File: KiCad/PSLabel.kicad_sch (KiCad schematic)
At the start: 0 parts

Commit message: Refactor code structure for improved readability and maintainability
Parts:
- added U1: nRF54L15-QFXX, Package_DFN_QFN:QFN-48-1EP_6x6mm_P0.4mm_EP4.6x4.6mm, symbol nordic-lib-kicad-nrf54l:nRF54L15-QFXX
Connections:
- new net: U1.10 (VDD), U1.22 (VDD), U1.36 (VDD), U1.47 (VDD), U1.48 (VDD)
- new net: U1.32 (VSS_PA), U1.44 (VSS), U1.49 (VSS)
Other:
- title: (none) -> PSLabel
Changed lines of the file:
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@@
 	(generator_version "9.0")
 	(paper "A4")
+	(title_block
+		(title "PSLabel")
+		(date "2025-06-19")
+	)
+	(symbol
+		(lib_id "nordic-lib-kicad-nrf54l:nRF54L15-QFXX")
+		(at 132.08 101.6 0)
+		(unit 1)
+		(exclude_from_sim no)
+		(in_bom yes)
+		(on_board yes)
+		(dnp no)
+		(fields_autoplaced yes)
+		(property "Reference" "U1"
+			(at 132.08 101.6 0)
+			(do_not_autoplace yes)
+			(effects
+				(font
+					(size 1.27 1.27)
+				)
+			)
+		)
+		(property "Value" "nRF54L15-QFXX"
+			(at 132.08 104.14 0)
+			(do_not_autoplace yes)
+			(effects
+				(font
+					(size 1.27 1.27)
+				)
+			)
+		)
+		(property "Footprint" "Package_DFN_QFN:QFN-48-1EP_6x6mm_P0.4mm_EP4.6x4.6mm"
+			(at 132.08 175.26 0)
+			(effects
+				(font
+					(size 1.27 1.27)
+				)
+				(hide yes)
+			)
+		)
+		(property "Datasheet" "https://docs.nordicsemi.com/bundle/ps_nrf54L15"
+			(at 132.08 177.8 0)
+			(effects
+				(font
+					(size 1.27 1.27)
+				)
+				(hide yes)
+			)
+		)
+		(property "Description" "nRF54L Dual Core Multiprotocol BLE SoC"
+			(at 132.08 172.72 0)
+			(effects
+				(font
+					(size 1.27 1.27)
+				)
+				(hide yes)
+			)
+		)
+		(pin "17"
+		)
+		(pin "15"
+		)
+		(pin "30"
+		)
+		(pin "10"
+		)
+		(pin "25"
+		)
+		(pin "9"
+		)
+		(pin "14"
+		)
+		(pin "1"
+		)
+		(pin "21"
+		)
+		(pin "43"
+		)
+		(pin "37"
+		)
+		(pin "20"
+		)
+		(pin "13"
+		)
+		(pin "12"
+		)
+		(pin "48"
+		)
+		(pin "36"
+		)
+		(pin "18"
+		)
+		(pin "2"
+		)
+		(pin "32"
+		)
+		(pin "41"
+		)
+		(pin "46"
+		)
+		(pin "31"
+		)
+		(pin "3"
+		)
+		(pin "33"
+		)
+		(pin "16"
+		)
+		(pin "39"
+		)
+		(pin "45"
+		)
+		(pin "40"
+		)
+		(pin "38"
+		)
+		(pin "47"
+		)
+		(pin "22"
+		)
+		(pin "23"
+		)
+		(pin "35"
+		)
+		(pin "34"
+		)
+		(pin "44"
+		)
+		(pin "49"
+		)
+		(pin "11"
+		)
+		(pin "26"
+		)
+		(pin "28"
+		)
+		(pin "7"
+		)
+		(pin "4"
+		)
+		(pin "6"
+		)
+		(pin "42"
+		)
+		(pin "8"
+		)
+		(pin "19"
+		)
+		(pin "5"
+		)
+		(pin "29"
+		)
+		(pin "24"
+		)
+		(pin "27"
+		)
+		(instances
+			(project ""
+				(path "/3e66aa7a-7b9f-4ef6-923c-a0fae49a7217"
+					(reference "U1")
+					(unit 1)
+				)
+			)
+		)
+	)
 	(sheet_instances
 		(path "/"

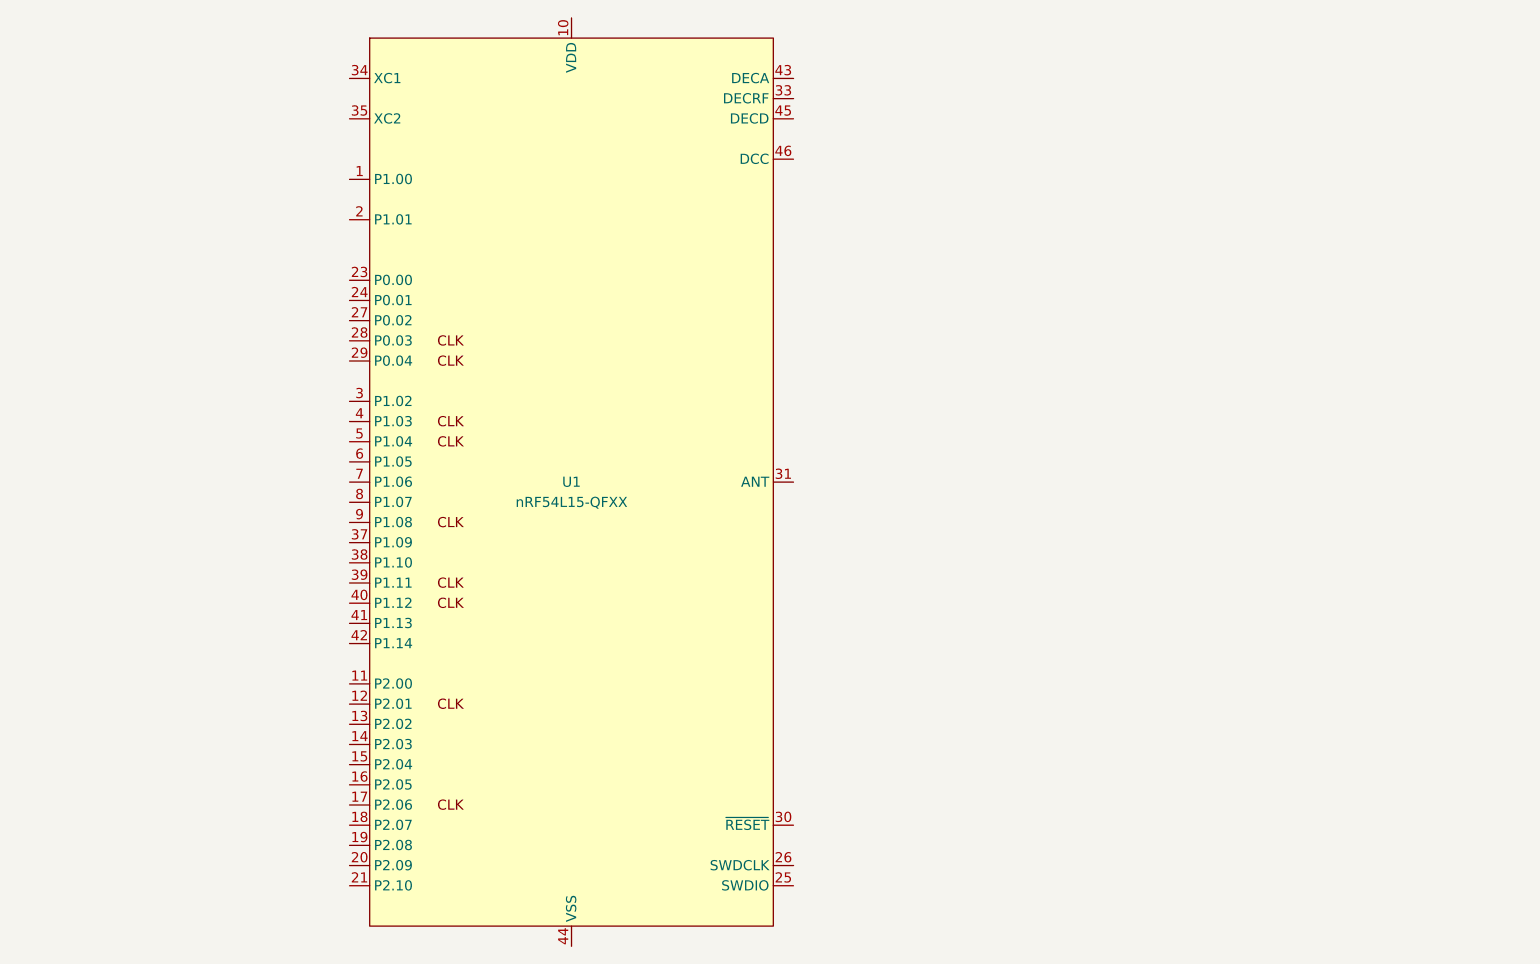
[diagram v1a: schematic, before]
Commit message: Add nRF54L15 schematic to KiCad project
- Introduced a new schematic file for the nRF54L15 component.
- Included detailed properties such as Reference, Value, Footprint, Datasheet, and Description.
- Defined multiple pins with their respective attributes and alternate functions.
- Ensured proper formatting and organization for readability and future modifications.
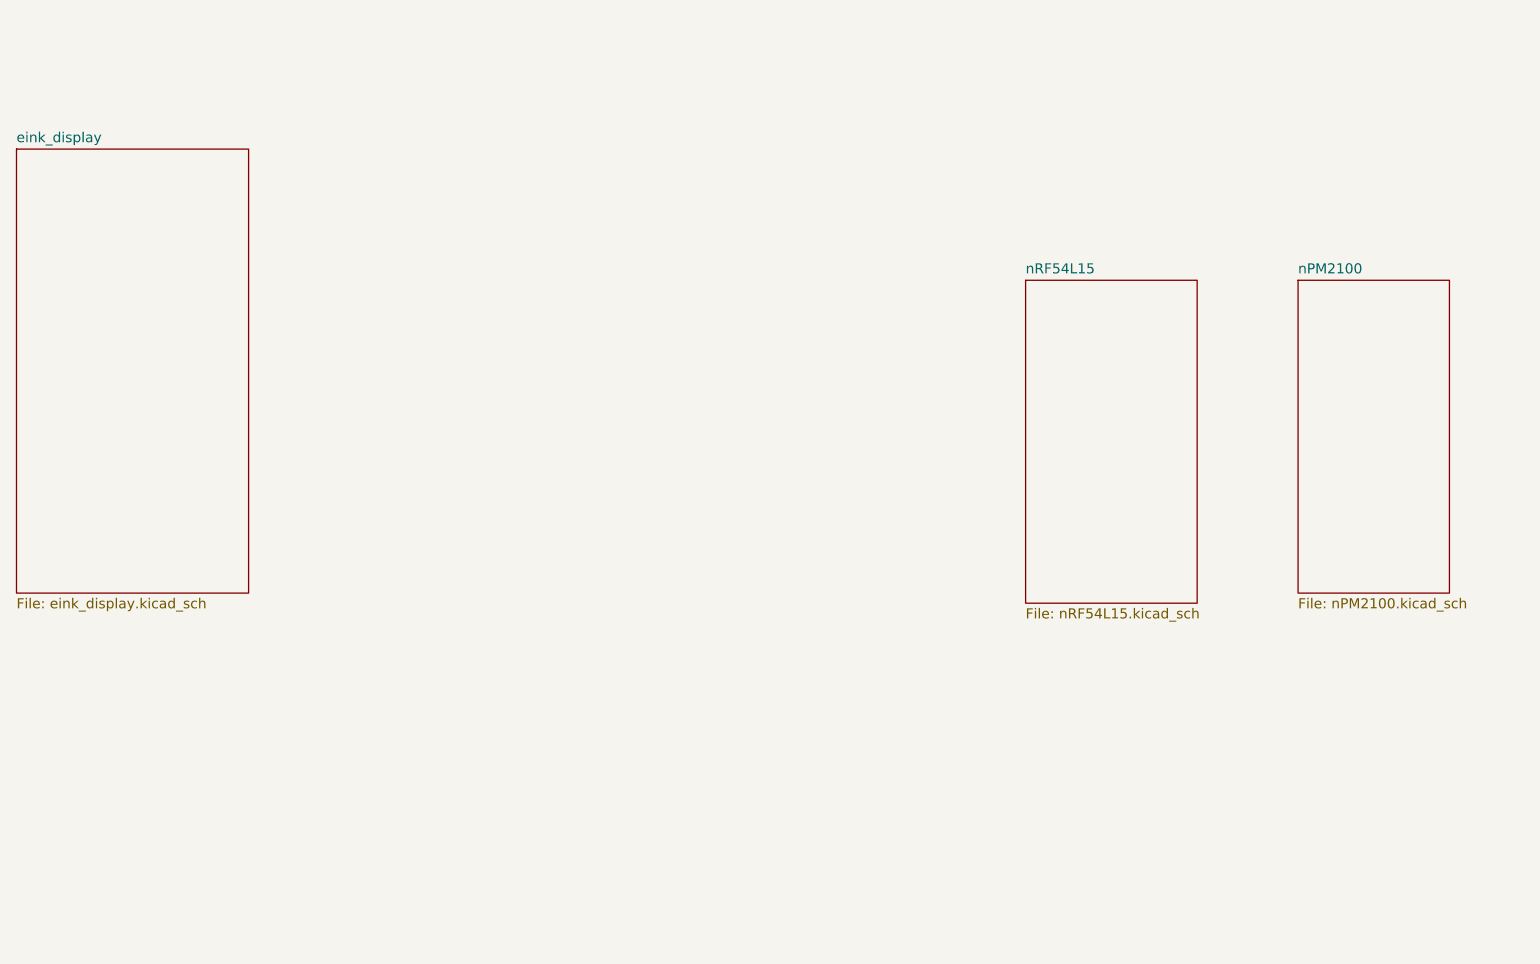
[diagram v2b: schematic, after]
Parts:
- removed U1: nRF54L15-QFXX, Package_DFN_QFN:QFN-48-1EP_6x6mm_P0.4mm_EP4.6x4.6mm, symbol nordic-lib-kicad-nrf54l:nRF54L15-QFXX
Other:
- added sheet eink_display (eink_display.kicad_sch)
- added sheet nPM2100 (nPM2100.kicad_sch)
- added sheet nRF54L15 (nRF54L15.kicad_sch)
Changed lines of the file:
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@@
 		(date "2025-06-19")
 	)
-	(symbol
-		(lib_id "nordic-lib-kicad-nrf54l:nRF54L15-QFXX")
-		(at 132.08 101.6 0)
-		(unit 1)
+	(sheet
+		(at 62.23 59.69)
+		(size 29.21 55.88)
 		(exclude_from_sim no)
 		(in_bom yes)
@@
 		(dnp no)
 		(fields_autoplaced yes)
-		(property "Reference" "U1"
-			(at 132.08 101.6 0)
-			(do_not_autoplace yes)
+		(stroke
+			(width 0.1524)
+			(type solid)
+		)
+		(fill
+			(color 0 0 0 0.0000)
+		)
+		(property "Sheetname" "eink_display"
+			(at 62.23 58.9784 0)
 			(effects
 				(font
 					(size 1.27 1.27)
 				)
+				(justify left bottom)
 			)
 		)
-		(property "Value" "nRF54L15-QFXX"
-			(at 132.08 104.14 0)
-			(do_not_autoplace yes)
+		(property "Sheetfile" "eink_display.kicad_sch"
+			(at 62.23 116.1546 0)
 			(effects
 				(font
 					(size 1.27 1.27)
 				)
+				(justify left top)
 			)
 		)
-		(property "Footprint" "Package_DFN_QFN:QFN-48-1EP_6x6mm_P0.4mm_EP4.6x4.6mm"
-			(at 132.08 175.26 0)
+		(instances
+			(project "PSLabel"
+				(path "/3e66aa7a-7b9f-4ef6-923c-a0fae49a7217"
+					(page "4")
+				)
+			)
+		)
+	)
+	(sheet
+		(at 223.52 76.2)
+		(size 19.05 39.37)
+		(exclude_from_sim no)
+		(in_bom yes)
+		(on_board yes)
+		(dnp no)
+		(fields_autoplaced yes)
+		(stroke
+			(width 0.1524)
+			(type solid)
+		)
+		(fill
+			(color 0 0 0 0.0000)
+		)
+		(property "Sheetname" "nPM2100"
+			(at 223.52 75.4884 0)
 			(effects
 				(font
 					(size 1.27 1.27)
 				)
-				(hide yes)
+				(justify left bottom)
 			)
 		)
-		(property "Datasheet" "https://docs.nordicsemi.com/bundle/ps_nrf54L15"
-			(at 132.08 177.8 0)
+		(property "Sheetfile" "nPM2100.kicad_sch"
+			(at 223.52 116.1546 0)
 			(effects
 				(font
 					(size 1.27 1.27)
 				)
-				(hide yes)
+				(justify left top)
 			)
 		)
-		(property "Description" "nRF54L Dual Core Multiprotocol BLE SoC"
-			(at 132.08 172.72 0)
+		(instances
+			(project "PSLabel"
+				(path "/3e66aa7a-7b9f-4ef6-923c-a0fae49a7217"
+					(page "3")
+				)
+			)
+		)
+	)
+	(sheet
+		(at 189.23 76.2)
+		(size 21.59 40.64)
+		(exclude_from_sim no)
+		(in_bom yes)
+		(on_board yes)
+		(dnp no)
+		(fields_autoplaced yes)
+		(stroke
+			(width 0.1524)
+			(type solid)
+		)
+		(fill
+			(color 0 0 0 0.0000)
+		)
+		(property "Sheetname" "nRF54L15"
+			(at 189.23 75.4884 0)
 			(effects
 				(font
 					(size 1.27 1.27)
 				)
-				(hide yes)
+				(justify left bottom)
 			)
 		)
-		(pin "17"
-		)
-		(pin "15"
-		)
-		(pin "30"
-		)
-		(pin "10"
-		)
-		(pin "25"
-		)
-		(pin "9"
-		)
-		(pin "14"
-		)
-		(pin "1"
-		)
-		(pin "21"
-		)
-		(pin "43"
-		)
-		(pin "37"
-		)
-		(pin "20"
-		)
-		(pin "13"
-		)
-		(pin "12"
-		)
-		(pin "48"
-		)
-		(pin "36"
-		)
-		(pin "18"
-		)
-		(pin "2"
-		)
-		(pin "32"
-		)
-		(pin "41"
-		)
-		(pin "46"
-		)
-		(pin "31"
-		)
-		(pin "3"
-		)
-		(pin "33"
-		)
-		(pin "16"
-		)
-		(pin "39"
-		)
-		(pin "45"
-		)
-		(pin "40"
-		)
-		(pin "38"
-		)
-		(pin "47"
-		)
-		(pin "22"
-		)
-		(pin "23"
-		)
-		(pin "35"
-		)
-		(pin "34"
-		)
-		(pin "44"
-		)
-		(pin "49"
-		)
-		(pin "11"
-		)
-		(pin "26"
-		)
-		(pin "28"
-		)
-		(pin "7"
-		)
-		(pin "4"
-		)
-		(pin "6"
-		)
-		(pin "42"
-		)
-		(pin "8"
-		)
-		(pin "19"
-		)
-		(pin "5"
-		)
-		(pin "29"
-		)
-		(pin "24"
-		)
-		(pin "27"
+		(property "Sheetfile" "nRF54L15.kicad_sch"
+			(at 189.23 117.4246 0)
+			(effects
+				(font
+					(size 1.27 1.27)
+				)
+				(justify left top)
+			)
 		)
 		(instances
-			(project ""
+			(project "PSLabel"
 				(path "/3e66aa7a-7b9f-4ef6-923c-a0fae49a7217"
-					(reference "U1")
-					(unit 1)
+					(page "2")
 				)
 			)
